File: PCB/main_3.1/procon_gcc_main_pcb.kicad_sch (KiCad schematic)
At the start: 129 parts, among them J1 Conn_01x04_Pin, J2 SM02B-SURS-TF_LF__SN_, J3 To Button Board, J4 SM02B-SURS-TF_LF__SN_, J5 Conn_01x02_Pin, J9 USB_C_Receptacle, Q4 BSS138DW, Q5 BSS138DW, Q7 MMBT3904, Q8 MMBT3904, SW1 1TS026A-1000-0550, SW1 GL18_SW, SW2 GL18_SW, SW4 TS35CA, T1 36-8730, T2 36-8730, T3 36-8730, T4 36-8730, U1 GH39F (Hall SOT23), U10 MCP3002, U11 ST_LSM6, U12 PI3USB4000A, U15 DRV2605LYZFR, U16 BQ25180, U2 GD25Q80EEIGR, U2 GH39F (Hall SOT23), U3 GH39F (Hall SOT23), U4 GH39F (Hall SOT23), U4 TPS630001RCR, U5 ST_LSM6, U6 RP2040, U7 CH340K, U8 MCP3002, U9 ESP32-PICO-MINI-02, Y1 Crystal_GND3

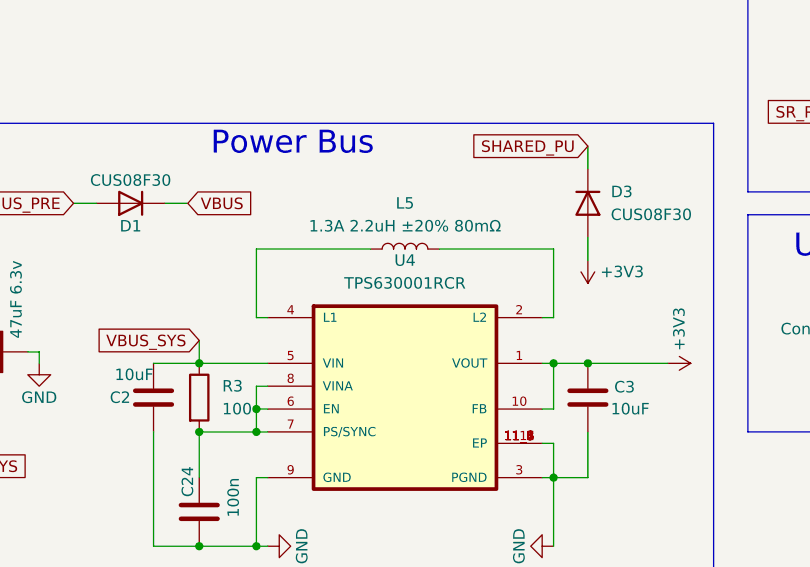
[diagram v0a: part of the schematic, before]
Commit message: Changes to remove debug code
- Remove debug smoothing of value 16 (Should have been 4 on mainline)
- Disable PMIC voltage regulation (Two switching regulators were stacking, adding noise to the voltage readings on the analog sticks)
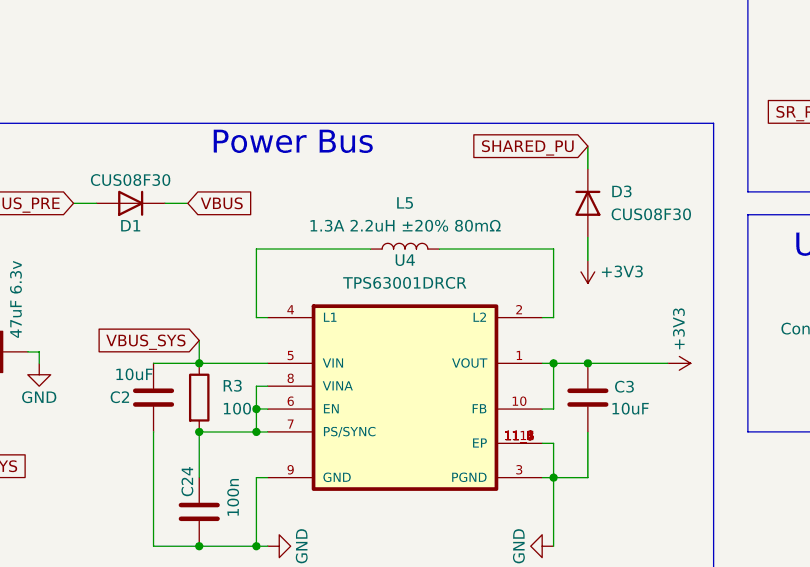
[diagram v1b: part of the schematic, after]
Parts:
- U4: value TPS630001RCR -> TPS63001DRCR
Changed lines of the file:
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@@
 			)
 		)
-		(property "Value" "TPS630001RCR"
+		(property "Value" "TPS63001DRCR"
 			(at 132.08 168.91 0)
 			(effects

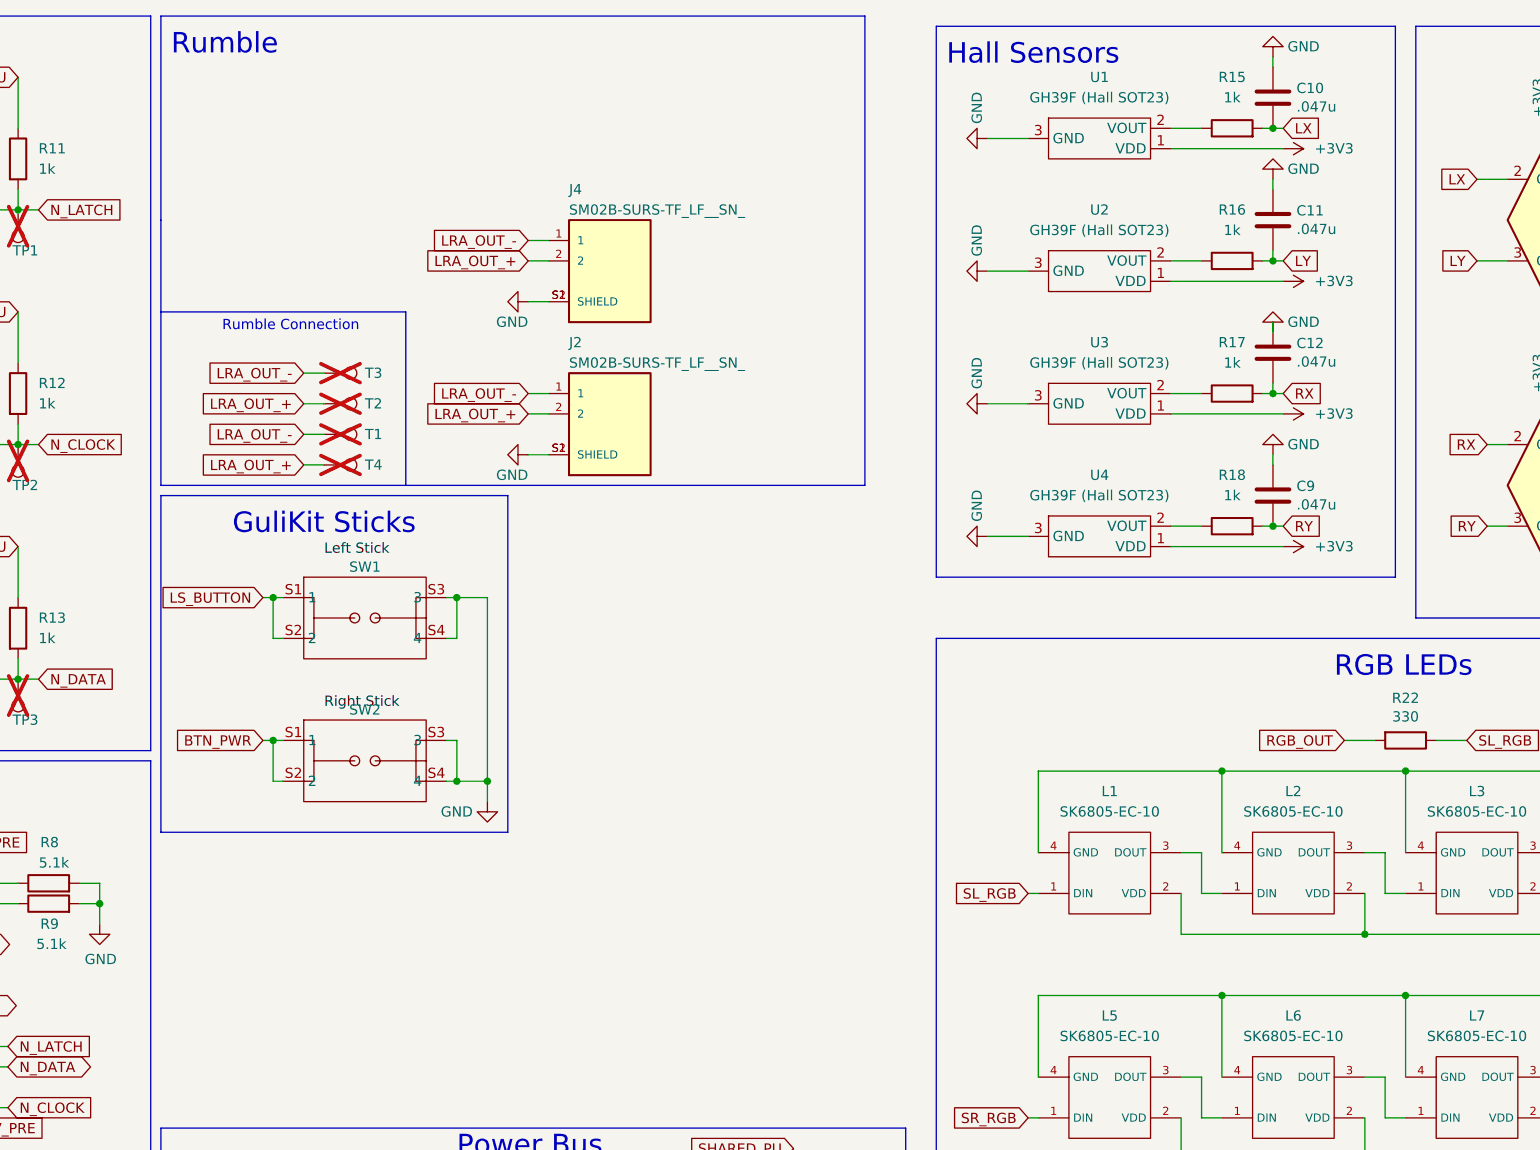
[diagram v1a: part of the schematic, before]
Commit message: PCB revision
- Exchange G18 sticks for newer iteration with TMR sensing
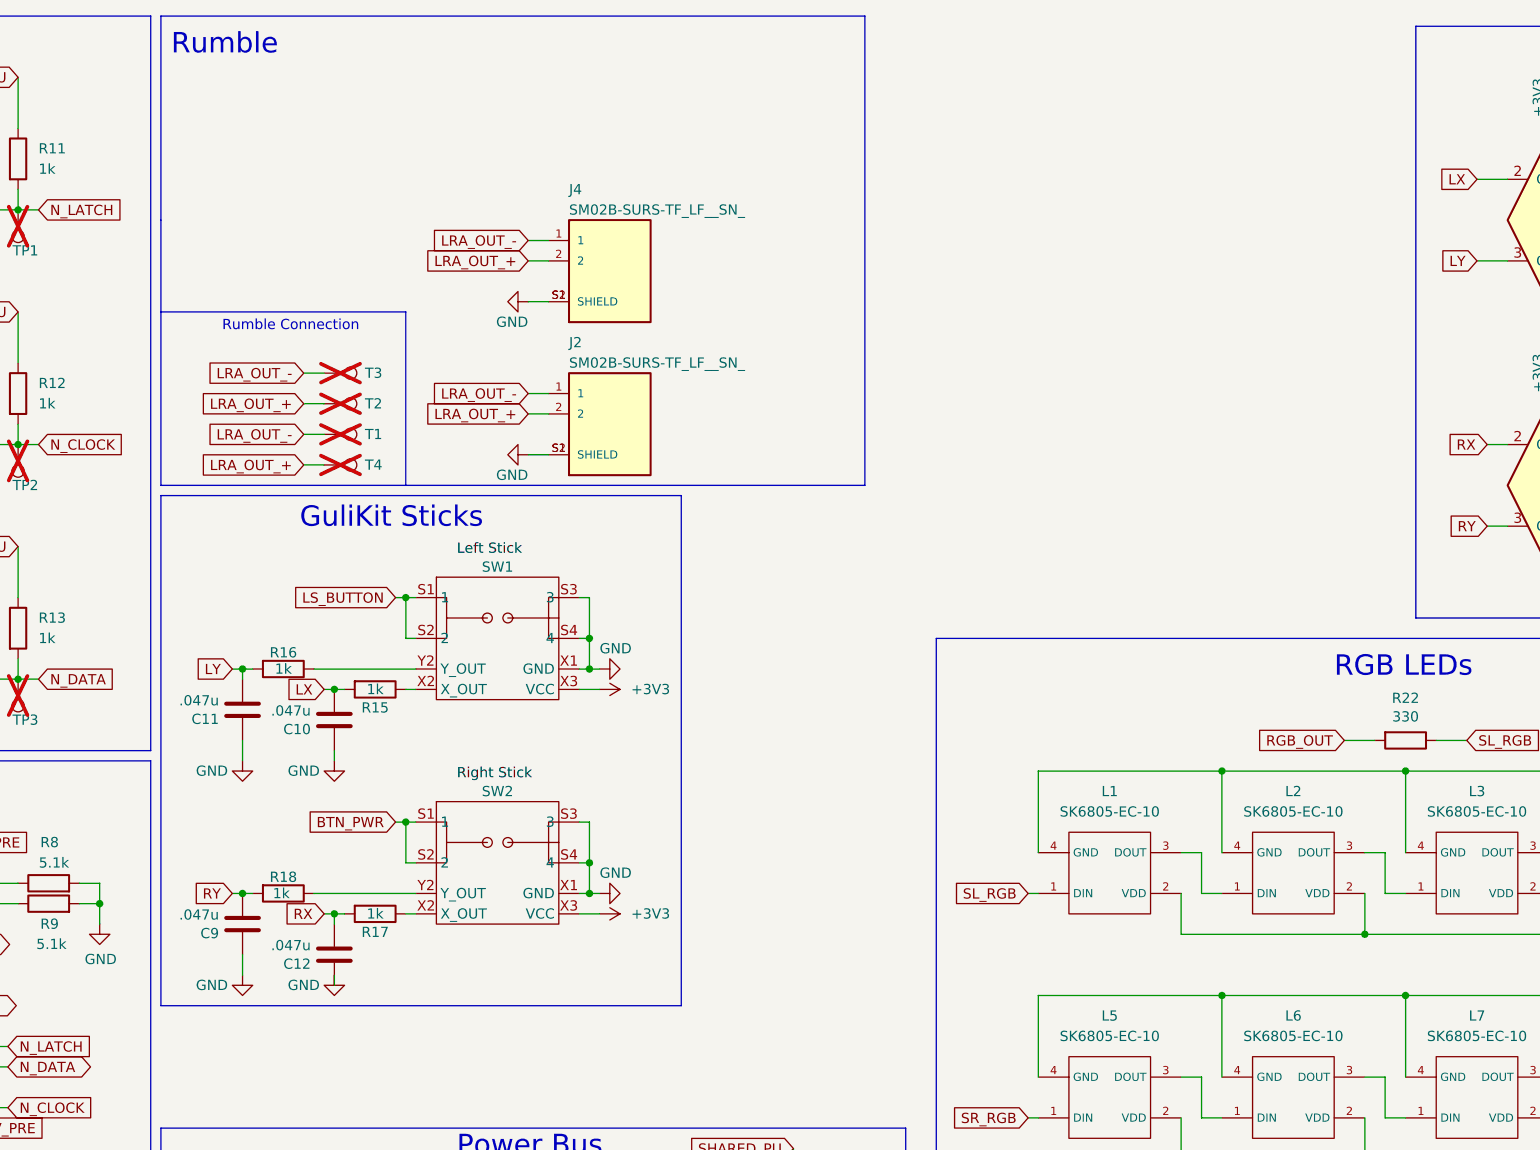
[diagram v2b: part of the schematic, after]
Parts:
- removed U1, U2, U3, U4: GH39F (Hall SOT23), hhl:GH39F, symbol progcc_v3:GH39F (Hall SOT23)
- SW1, SW2: value GL18_SW -> GL1807SYAE-002; footprint hhl:GL18 -> hhl:GL1807SYAE; symbol progcc_v3:GL18_SW -> progcc_v3:GL1807SYAE-002; MPN GL18 -> GL1807SYAE-002
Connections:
- net +3V3: now also SW1.X3 (VCC), SW1.Y3 (VCC), SW2.X3 (VCC), SW2.Y3 (VCC)
- net GND: now also SW1.X1 (GND), SW1.Y1 (GND), SW2.X1 (GND), SW2.Y1 (GND)
- net at R18.1: now also SW2.Y2 (Y_OUT)
- net at R16.1: now also SW1.Y2 (Y_OUT)
- net at R15.1: now also SW1.X2 (X_OUT)
- net at R17.1: now also SW2.X2 (X_OUT)
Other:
- note removed: "Hall Sensors"
- moved on the sheet: C10, C11, C12, C9, R15, R16, R17, R18
